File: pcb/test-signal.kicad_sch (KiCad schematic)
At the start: 36 parts, among them J5 731000105, U84 FSA553UCX, U85 LM27761DSGR, U87 AD5683RARMZ, U94 MAX4489AUA+

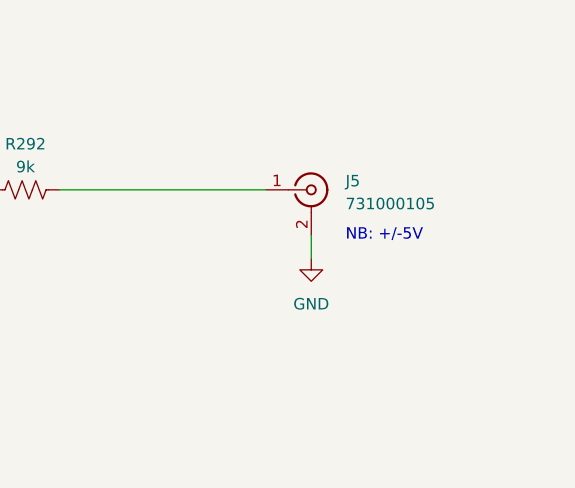
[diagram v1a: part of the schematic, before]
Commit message: Update part numbers
Replace OEPSPN 'OEPS020171' with 'OEPS020223'.
Correct component Value and MPN by adding a leading zero ('731000105' -> '0731000105').
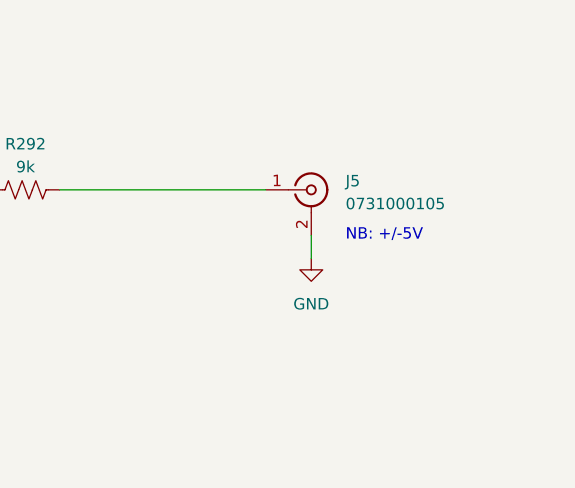
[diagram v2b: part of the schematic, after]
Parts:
- J5: value 731000105 -> 0731000105; MPN 731000105 -> 0731000105
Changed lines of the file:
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@@
 			)
 		)
-		(property "Value" "731000105"
+		(property "Value" "0731000105"
 			(at 252.73 35.8532 0)
 			(show_name no)
@@
 			)
 		)
-		(property "MPN" "731000105"
+		(property "MPN" "0731000105"
 			(at 248.92 34.29 0)
 			(hide yes)

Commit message: Added 'Description' to all the components
Updated PCB accordingly.
Configured files for manufacturing generation according to standards.
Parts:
- C100, C101, C97: OEPS Description (none) -> CAPACITOR: SMD CER 1206 4.7uF 16V ±10% X7R [CL31B475KOHNNNE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
- C102, C103, C106: OEPS Description (none) -> CAPACITOR: SMD CER 0402 100nF 25V ±10% X7R (OEPS H02 001) [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
- C104, C99: OEPS Description (none) -> CAPACITOR: SMD CER 0402 10nF 25V ±10% X7R (OEPS H1 002) [GR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
- C105: OEPS Description (none) -> CAPACITOR: SMD CER 1206 10uF 50V ±10% X7R [CL31B106KBHNNNE]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
- C128: OEPS Description (none) -> CAPACITOR: SMD CER 0402 100pF 50V ±5% C0G [CC0402JRNPO9BN10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
- C129, C131, C96: OEPS Description (none) -> CAPACITOR: SMD CER 0402 1.8nF 50V ±5% X7R [C0402C182J5RACTU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
- C130, C132: OEPS Description (none) -> DNP: Do Not Populate (DNI)
- C98: OEPS Description (none) -> CAPACITOR: SMD CER 0603 1uF 25V ±10% X5R [CL10A105KA8NNNC] 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
- J5: OEPS Description (none) -> CONNECTOR: BNC JACK 50ohm R/A [0731000105] [TH]
- R267, R291: OEPS Description (none) -> RESISTOR: SMD 0402 100kΩ ±1% 0.063W [AC0402FR-07100KL] [SMD]
- R268: OEPS Description (none) -> RESISTOR: SMD 0402 249kΩ ±1% 0.063W [RMCF0402FT249K] [SMD]
- R269, R293, R294, R298, R299, R300: OEPS Description (none) -> RESISTOR: SMD 0402 1kΩ ±0.1% 0.063W [RG1005P-102-B-T5] [SMD]
- R292: OEPS Description (none) -> RESISTOR: SMD 0805 9kΩ ±0.1% 0.125W [RT0805BRE079KL] [SMD]
- R295, R296: OEPS Description (none) -> RESISTOR: SMD 0402 10Ω ±1% 0.063W [RMCF0402FT10R0] [SMD]
- R297: OEPS Description (none) -> RESISTOR: SMD 0402 5kΩ ±0.1% 0.050W [PNM0402E5001BST1] [SMD]
- U84: OEPS Description (none) -> IC: AUDIO SWITCH SPST DUAL [FSA553UCX] [9-WLCSP]
- U85: OEPS Description (none) -> IC: Switched-capacitor Voltage Inverter [LM27761DSGR] [8-WS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
- U87: OEPS Description (none) -> IC: DAC 16BIT [AD5683RARMZ] [10-MSOP]
- U94: OEPS Description (none) -> IC: OPAMP GP 2 CIRCUIT [MAX4489AUA+] [8-MSOP]
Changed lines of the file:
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@@
 			)
 		)
+		(property "OEPS Description" "CAPACITOR:   SMD CER 1206 4.7uF 16V ±10% X7R   [CL31B475KOHNNNE] [SMD]" (at 133.35 167.64 0) (effects (font (size 1.27 1.27)) (hide yes)))
 	)
 	(symbol
@@
 			)
 		)
+		(property "OEPS Description" "CAPACITOR:   SMD CER 0402 1.8nF 50V ±5% X7R   [C0402C182J5RACTU] [SMD]" (at 133.35 115.57 0) (effects (font (size 1.27 1.27)) (hide yes)))
 	)
 	(symbol
@@
 			)
 		)
+		(property "OEPS Description" "IC:   OPAMP GP 2 CIRCUIT   [MAX4489AUA+] [8-MSOP]" (at 161.29 36.83 0) (effects (font (size 1.27 1.27)) (hide yes)))
 	)
 	(symbol
@@
 			)
 		)
+		(property "OEPS Description" "DNP: Do Not Populate (DNI)" (at 157.48 73.66 0) (effects (font (size 1.27 1.27)) (hide yes)))
 	)
 	(symbol
@@
 			)
 		)
+		(property "OEPS Description" "RESISTOR:   SMD 0402 1kΩ ±0.1% 0.063W   [RG1005P-102-B-T5] [SMD]" (at 195.58 104.14 0) (effects (font (size 1.27 1.27)) (hide yes)))
 	)
 	(symbol
@@
 			)
 		)
+		(property "OEPS Description" "CAPACITOR:   SMD CER 0402 100nF 25V ±10% X7R (OEPS H02 001)   [C1005X7R1E104K050BB] [SMD]" (at 152.4 48.26 0) (effects (font (size 1.27 1.27)) (hide yes)))
 	)
 	(symbol
@@
 			)
 		)
+		(property "OEPS Description" "CAPACITOR:   SMD CER 0402 1.8nF 50V ±5% X7R   [C0402C182J5RACTU] [SMD]" (at 157.48 62.23 0) (effects (font (size 1.27 1.27)) (hide yes)))
 	)
 	(symbol
@@
 			)
 		)
+		(property "OEPS Description" "CAPACITOR:   SMD CER 0402 100nF 25V ±10% X7R (OEPS H02 001)   [C1005X7R1E104K050BB] [SMD]" (at 267.97 83.82 0) (effects (font (size 1.27 1.27)) (hide yes)))
 	)
 	(symbol
@@
 			)
 		)
+		(property "OEPS Description" "CAPACITOR:   SMD CER 0402 100nF 25V ±10% X7R (OEPS H02 001)   [C1005X7R1E104K050BB] [SMD]" (at 152.4 26.67 0) (effects (font (size 1.27 1.27)) (hide yes)))
 	)
 	(symbol
@@
 			)
 		)
+		(property "OEPS Description" "IC:   AUDIO SWITCH SPST DUAL   [FSA553UCX] [9-WLCSP]" (at 80.01 34.29 0) (effects (font (size 1.27 1.27)) (hide yes)))
 	)
 	(symbol
@@
 			)
 		)
+		(property "OEPS Description" "IC:   OPAMP GP 2 CIRCUIT   [MAX4489AUA+] [8-MSOP]" (at 163.83 36.83 0) (effects (font (size 1.27 1.27)) (hide yes)))
 	)
 	(symbol
@@
 			)
 		)
+		(property "OEPS Description" "RESISTOR:   SMD 0402 1kΩ ±0.1% 0.063W   [RG1005P-102-B-T5] [SMD]" (at 157.48 82.55 0) (effects (font (size 1.27 1.27)) (hide yes)))
 	)
 	(symbol
@@
 			)
 		)
+		(property "OEPS Description" "RESISTOR:   SMD 0402 100kΩ ±1% 0.063W   [AC0402FR-07100KL] [SMD]" (at 115.57 162.56 0) (effects (font (size 1.27 1.27)) (hide yes)))
 	)
 	(symbol
@@
 			)
 		)
+		(property "OEPS Description" "RESISTOR:   SMD 0402 10Ω ±1% 0.063W   [RMCF0402FT10R0] [SMD]" (at 127 36.83 0) (effects (font (size 1.27 1.27)) (hide yes)))
 	)
 	(symbol
@@
 			)
 		)
+		(property "OEPS Description" "RESISTOR:   SMD 0402 249kΩ ±1% 0.063W   [RMCF0402FT249K] [SMD]" (at 97.79 175.26 0) (effects (font (size 1.27 1.27)) (hide yes)))
 	)
 	(symbol
@@
 			)
 		)
+		(property "OEPS Description" "IC:   Switched-capacitor Voltage Inverter   [LM27761DSGR] [8-WSON]" (at 69.85 165.1 0) (effects (font (size 1.27 1.27)) (hide yes)))
 	)
 	(symbol
@@
 			)
 		)
+		(property "OEPS Description" "IC:   DAC 16BIT   [AD5683RARMZ] [10-MSOP]" (at 220.98 104.14 0) (effects (font (size 1.27 1.27)) (hide yes)))
 	)
 	(symbol
@@
 			)
 		)
+		(property "OEPS Description" "RESISTOR:   SMD 0402 1kΩ ±0.1% 0.063W   [RG1005P-102-B-T5] [SMD]" (at 175.26 114.3 0) (effects (font (size 1.27 1.27)) (hide yes)))
 	)
 	(symbol
@@
 			)
 		)
+		(property "OEPS Description" "CAPACITOR:   SMD CER 0402 10nF 25V ±10% X7R (OEPS H1 002)   [GRM155R71E103KA01D] [SMD]" (at 86.36 85.09 0) (effects (font (size 1.27 1.27)) (hide yes)))
 	)
 	(symbol
@@
 			)
 		)
+		(property "OEPS Description" "RESISTOR:   SMD 0402 10Ω ±1% 0.063W   [RMCF0402FT10R0] [SMD]" (at 113.03 106.68 0) (effects (font (size 1.27 1.27)) (hide yes)))
 	)
 	(symbol
@@
 			)
 		)
+		(property "OEPS Description" "RESISTOR:   SMD 0402 5kΩ ±0.1% 0.050W   [PNM0402E5001BST1] [SMD]" (at 163.83 137.16 0) (effects (font (size 1.27 1.27)) (hide yes)))
 	)
 	(symbol
@@
 			)
 		)
+		(property "OEPS Description" "RESISTOR:   SMD 0402 1kΩ ±0.1% 0.063W   [RG1005P-102-B-T5] [SMD]" (at 133.35 137.16 0) (effects (font (size 1.27 1.27)) (hide yes)))
 	)
 	(symbol
@@
 			)
 		)
+		(property "OEPS Description" "CONNECTOR:   BNC JACK 50ohm R/A   [0731000105] [TH]" (at 248.92 34.29 0) (effects (font (size 1.27 1.27)) (hide yes)))
 	)
 	(symbol
@@
 			)
 		)
+		(property "OEPS Description" "CAPACITOR:   SMD CER 1206 10uF 50V ±10% X7R   [CL31B106KBHNNNE] [SMD]" (at 257.81 83.82 0) (effects (font (size 1.27 1.27)) (hide yes)))
 	)
 	(symbol
@@
 			)
 		)
+		(property "OEPS Description" "CAPACITOR:   SMD CER 0402 100pF 50V ±5% C0G   [CC0402JRNPO9BN101] [SMD]" (at 191.77 45.72 0) (effects (font (size 1.27 1.27)) (hide yes)))
 	)
 	(symbol
@@
 			)
 		)
+		(property "OEPS Description" "CAPACITOR:   SMD CER 1206 4.7uF 16V ±10% X7R   [CL31B475KOHNNNE] [SMD]" (at 85.09 173.99 0) (effects (font (size 1.27 1.27)) (hide yes)))
 	)
 	(symbol
@@
 			)
 		)
+		(property "OEPS Description" "CAPACITOR:   SMD CER 0402 10nF 25V ±10% X7R (OEPS H1 002)   [GRM155R71E103KA01D] [SMD]" (at 233.68 85.09 0) (effects (font (size 1.27 1.27)) (hide yes)))
 	)
 	(symbol
@@
 			)
 		)
+		(property "OEPS Description" "CAPACITOR:   SMD CER 0603 1uF 25V ±10% X5R   [CL10A105KA8NNNC] [SMD]" (at 50.8 168.91 0) (effects (font (size 1.27 1.27)) (hide yes)))
 	)
 	(symbol
@@
 			)
 		)
+		(property "OEPS Description" "IC:   AUDIO SWITCH SPST DUAL   [FSA553UCX] [9-WLCSP]" (at 80.01 104.14 0) (effects (font (size 1.27 1.27)) (hide yes)))
 	)
 	(symbol
@@
 			)
 		)
+		(property "OEPS Description" "CAPACITOR:   SMD CER 0402 1.8nF 50V ±5% X7R   [C0402C182J5RACTU] [SMD]" (at 162.56 115.57 0) (effects (font (size 1.27 1.27)) (hide yes)))
 	)
 	(symbol
@@
 			)
 		)
+		(property "OEPS Description" "DNP: Do Not Populate (DNI)" (at 133.35 127 0) (effects (font (size 1.27 1.27)) (hide yes)))
 	)
 	(symbol
@@
 			)
 		)
+		(property "OEPS Description" "RESISTOR:   SMD 0402 1kΩ ±0.1% 0.063W   [RG1005P-102-B-T5] [SMD]" (at 204.47 44.45 0) (effects (font (size 1.27 1.27)) (hide yes)))
 	)
 	(symbol
@@
 			)
 		)
+		(property "OEPS Description" "RESISTOR:   SMD 0805 9kΩ ±0.1% 0.125W   [RT0805BRE079KL] [SMD]" (at 217.17 34.29 0) (effects (font (size 1.27 1.27)) (hide yes)))
 	)
 	(symbol
@@
 			)
 		)
+		(property "OEPS Description" "RESISTOR:   SMD 0402 1kΩ ±0.1% 0.063W   [RG1005P-102-B-T5] [SMD]" (at 184.15 104.14 0) (effects (font (size 1.27 1.27)) (hide yes)))
 	)
 	(symbol
@@
 			)
 		)
+		(property "OEPS Description" "RESISTOR:   SMD 0402 100kΩ ±1% 0.063W   [AC0402FR-07100KL] [SMD]" (at 105.41 162.56 0) (effects (font (size 1.27 1.27)) (hide yes)))
 	)
 	(symbol
@@
 			)
 		)
+		(property "OEPS Description" "IC:   OPAMP GP 2 CIRCUIT   [MAX4489AUA+] [8-MSOP]" (at 135.89 106.68 0) (effects (font (size 1.27 1.27)) (hide yes)))
 	)
 	(symbol
@@
 			)
 		)
+		(property "OEPS Description" "CAPACITOR:   SMD CER 1206 4.7uF 16V ±10% X7R   [CL31B475KOHNNNE] [SMD]" (at 38.1 167.64 0) (effects (font (size 1.27 1.27)) (hide yes)))
 	)
 )
